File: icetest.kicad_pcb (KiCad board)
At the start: 2 copper layers, 66.7 x 57.2 mm, 61 parts, among them J1 R, J2 R, J3 R

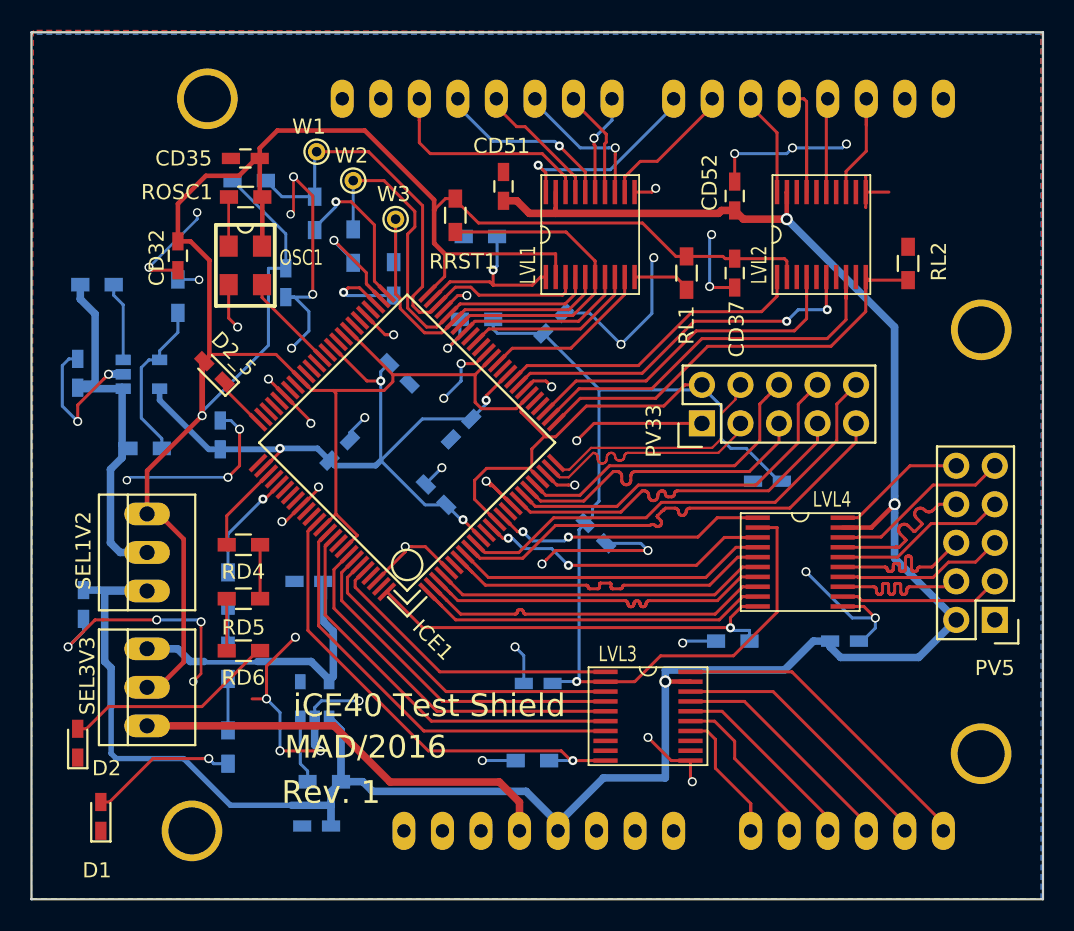
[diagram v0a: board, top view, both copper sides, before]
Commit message: more current for LEDs
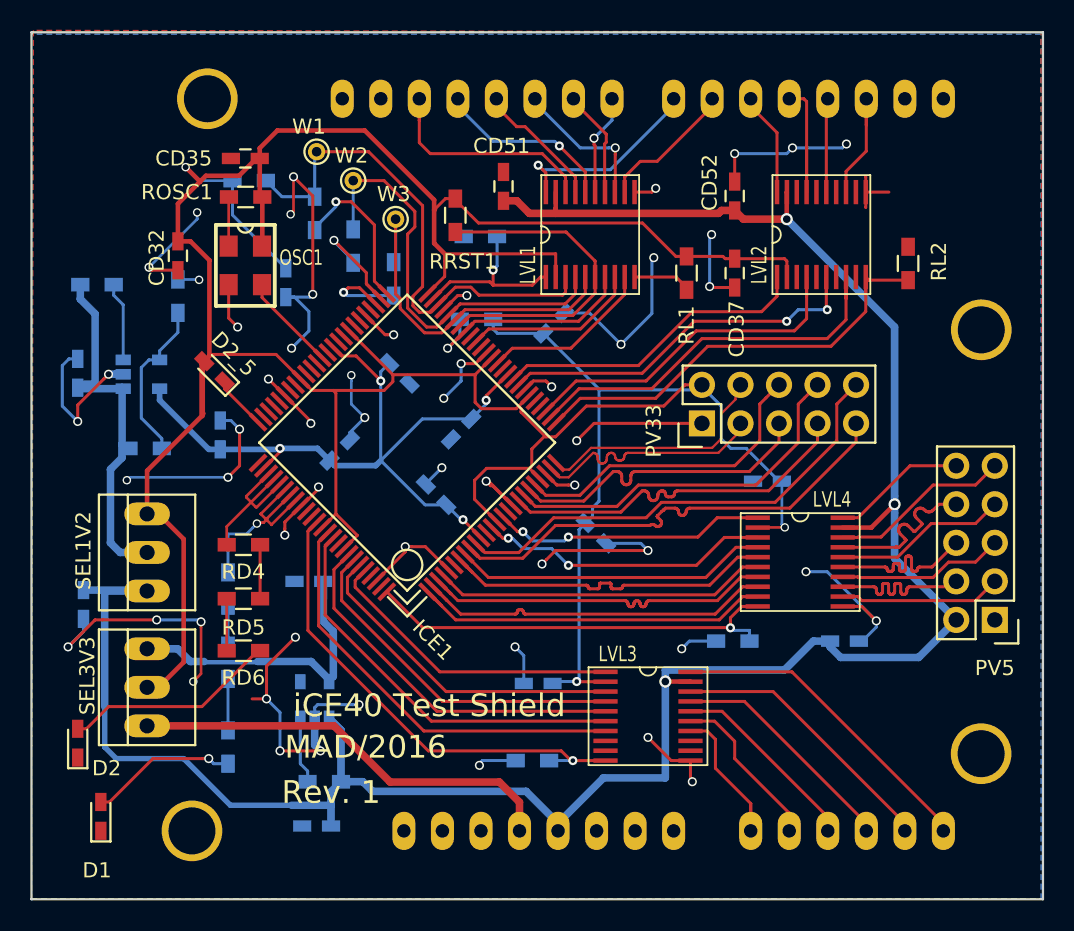
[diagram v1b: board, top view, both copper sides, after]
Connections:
- ICE1 pad 79: Net-(ICE1-Pad79) -> Net-(ICE1-Pad78)
- ICE1 pad 80: Net-(ICE1-Pad80) -> Net-(ICE1-Pad78)
- ICE1 pad 82: Net-(ICE1-Pad82) -> Net-(ICE1-Pad81)
- ICE1 pad 83: Net-(ICE1-Pad83) -> Net-(ICE1-Pad81)
- RD1 pad 1: Net-(ICE1-Pad80) -> Net-(ICE1-Pad81)
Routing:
- net +3V3: track 266.8 -> 243.8 mm, vias 2 -> 3
- net Net-(ICE1-Pad81): track 0.00 -> 13.3 mm, vias 0 -> 1
- net Net-(ICE1-Pad80): track 7.28 -> 0.00 mm, vias 1 -> 0
- net Net-(ICE1-Pad78): track 5.83 -> 10.9 mm
- net GND: track 193.5 -> 198.0 mm, vias 54 -> 55

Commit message: minor layout
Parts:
- removed J1, J2, J3: R, Resistors_SMD:R_0603_HandSoldering
- added W4: CDONE, Connect:PINTST, F.Cu at (146.8, 106.5)
- added W5: RST, Connect:PINTST, F.Cu at (145.7, 103.0)
- CD34, CD38: moved to F.Cu
- W1: value TEST_1P -> SCLK
- W2: value TEST_1P -> MISO
- W3: value TEST_1P -> MOSI
- moved CD34 28.8 mm to (132.7, 118.6), turned to 135 degrees
- moved CD38 28.6 mm to (130.2, 120.7), turned to 135 degrees
- moved RDON1 9.30 mm to (150.7, 103.1)
- moved W1 8.83 mm to (143.1, 110.0)
- moved W3 4.21 mm to (143.0, 106.0)
- moved W2 3.02 mm to (141.8, 101.6)
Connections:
- W2 pad 1: /Arduino Shield/MOSI -> /Arduino Shield/MISO
- W3 pad 1: /Arduino Shield/MISO -> /Arduino Shield/MOSI
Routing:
- net /Arduino Shield/ICE_RST: track 22.9 -> 38.7 mm, vias 0 -> 1
- net /Arduino Shield/ICE_CDONE: track 15.7 -> 27.4 mm
- net Net-(ICE1-Pad51): track 11.0 -> 0.97 mm, vias 1 -> 0
- net (no net): track 0.00 -> 8.85 mm, vias 0 -> 2
- net Net-(ICE1-Pad52): track 8.57 -> 0.00 mm, vias 1 -> 0
- net Net-(ICE1-Pad53): track 6.87 -> 0.00 mm, vias 1 -> 0
- net /Arduino Shield/MOSI: track 28.3 -> 22.8 mm, vias 0 -> 1
- net /Arduino Shield/SCK: track 34.2 -> 28.9 mm, vias 0 -> 1
- net +3V3: track 243.8 -> 249.0 mm, vias 3 -> 5
- net /Arduino Shield/MISO: track 24.0 -> 28.7 mm, vias 0 -> 1
- net GND: track 198.0 -> 193.9 mm, vias 55 -> 54
- net VCC: track 50.4 -> 51.7 mm
- net /Arduino Shield/aSCK: track 15.9 -> 15.1 mm

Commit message: add errata and notes
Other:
- board text added: "33V"
- board text added: "5V"
- board text added: "CDNE"
- board text added: "GND"
- board text added: "MISO"
- board text added: "MOSI"
- board text added: "RST"
- board text added: "SCK"
- board text added: "a33V"
- board text added: "r33V"
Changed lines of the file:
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@@
     (links 206)
     (no_connects 0)
-    (area 123.114999 93.269999 189.940001 150.570001)
+    (area 117.115001 50.227999 191.801534 156.163599)
     (thickness 1.6)
-    (drawings 11)
+    (drawings 26)
     (tracks 1805)
     (zones 0)
@@
     (pad_to_mask_clearance 0.2)
     (aux_axis_origin 0 0)
-    (visible_elements FFFFFF79)
+    (visible_elements FFFFFE79)
     (pcbplotparams
-      (layerselection 0x00030_80000001)
+      (layerselection 0x00120_00000001)
       (usegerberextensions false)
       (excludeedgelayer true)
@@
       (outputformat 4)
       (mirror false)
-      (drillshape 0)
+      (drillshape 2)
       (scaleselection 1)
-      (outputdirectory ""))
+      (outputdirectory /tmp))
   )
   (net 0 "")
@@
     )
   )
+  (gr_text 5V (at 120.269 130.4798) (layer Dwgs.User)
+    (effects (font (size 1.5 1.5) (thickness 0.3)))
+  )
+  (gr_text 33V (at 120.4214 125.1966) (layer Dwgs.User)
+    (effects (font (size 1.5 1.5) (thickness 0.3)))
+  )
+  (gr_text a33V (at 120.015 138.9126) (layer Dwgs.User)
+    (effects (font (size 1.5 1.5) (thickness 0.3)))
+  )
+  (gr_text 33V (at 120.3706 136.652) (layer Dwgs.User)
+    (effects (font (size 1.5 1.5) (thickness 0.3)))
+  )
+  (gr_text r33V (at 119.9134 134.1374) (layer Dwgs.User)
+    (effects (font (size 1.5 1.5) (thickness 0.3)))
+  )
+  (gr_text a33V (at 155.3972 153.2636 90) (layer Dwgs.User)
+    (effects (font (size 1.5 1.5) (thickness 0.3)))
+  )
+  (gr_text 5V (at 158.0134 153.3144 90) (layer Dwgs.User)
+    (effects (font (size 1.5 1.5) (thickness 0.3)))
+  )
+  (gr_text GND (at 163.1696 153.2636 90) (layer Dwgs.User)
+    (effects (font (size 1.5 1.5) (thickness 0.3)))
+  )
+  (gr_text GND (at 160.528 153.3398 90) (layer Dwgs.User)
+    (effects (font (size 1.5 1.5) (thickness 0.3)))
+  )
+  (gr_text RST (at 161.4678 90.17 90) (layer Dwgs.User)
+    (effects (font (size 1.5 1.5) (thickness 0.3)))
+  )
+  (gr_text CDNE (at 158.9532 90.1954 90) (layer Dwgs.User)
+    (effects (font (size 1.5 1.5) (thickness 0.3)))
+  )
+  (gr_text MOSI (at 153.8478 90.1446 90) (layer Dwgs.User)
+    (effects (font (size 1.5 1.5) (thickness 0.3)))
+  )
+  (gr_text MISO (at 151.3332 90.17 90) (layer Dwgs.User)
+    (effects (font (size 1.5 1.5) (thickness 0.3)))
+  )
+  (gr_text SCK (at 148.8948 90.551 90) (layer Dwgs.User)
+    (effects (font (size 1.5 1.5) (thickness 0.3)))
+  )
+  (gr_text GND (at 146.2786 90.424 90) (layer Dwgs.User)
+    (effects (font (size 1.5 1.5) (thickness 0.3)))
+  )
   (gr_text "Rev. 1" (at 174.117 109.4105) (layer B.SilkS)

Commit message: redo layout
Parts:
- removed LVL1, LVL2, LVL3, LVL4: txb0108, local:PSO_20
- removed RCLK1, RL1, RL2, RL3, RL4: 10k, Resistors_SMD:R_0603_HandSoldering
- added P0: CONN_02X04, Pin_Headers:Pin_Header_Straight_2x05, F.Cu at (161.5, 141.2)
- added P11: CONN_02X04, Pin_Headers:Pin_Header_Straight_2x05, F.Cu at (139.2, 106.2)
- added P12: CONN_02X04, Pin_Headers:Pin_Header_Straight_2x05, F.Cu at (138.7, 133.1)
- added P2: CONN_02X04, Pin_Headers:Pin_Header_Straight_2x05, F.Cu at (185.9, 102.6)
- added RSCK1: 10k, Resistors_SMD:R_0603_HandSoldering, F.Cu at (144.8, 103.6)
- added RU3: 10k, Resistors_SMD:R_0603_HandSoldering, B.Cu at (161.0, 108.3)
- added RU4: 10k, Resistors_SMD:R_0603_HandSoldering, F.Cu at (168.1, 104.1)
- added UL1: sn74lvc2t45, local:VSSOP-8, F.Cu at (148.6, 104.1)
- added UL2: sn74lvc2t45, local:VSSOP-8, F.Cu at (153.7, 104.1)
- added UL3: sn74lvc2t45, local:VSSOP-8, F.Cu at (158.8, 104.1)
- added UL4: sn74lvc2t45, local:VSSOP-8, F.Cu at (163.8, 104.1)
- added UL5: sn74lvc2t45, local:VSSOP-8, F.Cu at (176.3, 137.2)
- added UL6: sn74lvc2t45, local:VSSOP-8, F.Cu at (177.3, 132.6)
- added UL7: sn74lvc2t45, local:VSSOP-8, F.Cu at (175.3, 128.3)
- added UL8: sn74lvc2t45, local:VSSOP-8, F.Cu at (177.3, 124.5)
- added W12: TEST_1P, Connect:PINTST, F.Cu at (135.6, 120.4)
- CD32, CD34, CD37, CD38, CD51, D2_5, RRST1: moved to B.Cu
- CD53: moved to F.Cu
- SEL1V2, SEL3V3: footprint Connect:PINHEAD1-3 -> Pin_Headers:Pin_Header_Straight_1x03
- moved CD53 52.7 mm to (178.3, 141.2), turned to 0 degrees
- moved CD34 43.3 mm to (172.2, 136.1), turned to 180 degrees
- moved CD32 30.4 mm to (155.8, 128.0), turned to 90 degrees
- moved CD38 28.5 mm to (158.7, 121.8), turned to 270 degrees
- moved D2 21.1 mm to (147.2, 142.5), turned to 0 degrees
- moved D2_5 20.7 mm to (144.8, 134.1), turned to 270 degrees
- moved RD1 17.7 mm to (152.9, 135.6), turned to 0 degrees
- moved OSC1 17.6 mm to (140.7, 126.0)
- moved RD4 17.5 mm to (152.4, 135.6)
- moved CD54 17.2 mm to (184.9, 118.4), turned to 90 degrees
- moved RD2 17.1 mm to (152.9, 138.2), turned to 180 degrees
- moved ROSC1 17.0 mm to (140.7, 120.9)
- moved RD5 17.0 mm to (152.4, 138.2)
- moved RD3 16.8 mm to (152.9, 140.7), turned to 0 degrees
- moved CD36 16.6 mm to (151.2, 120.5), turned to 270 degrees
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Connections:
- ARD1 pad 20: Net-(ARD1-Pad20) -> /Arduino Shield/aD5
- ARD1 pad 22: /Arduino Shield/aD7 -> Net-(ARD1-Pad22)
- ICE1 pad 10: /FPGA/D5- -> /FPGA/DIR5
- ICE1 pad 100: Net-(ICE1-Pad100) -> /FPGA/DIR1
- ICE1 pad 12: Net-(ICE1-Pad12) -> /FPGA/D5+
- ICE1 pad 13: Net-(ICE1-Pad13) -> /FPGA/D5-
- ICE1 pad 15: Net-(ICE1-Pad15) -> /FPGA/D7+
- ICE1 pad 16: Net-(ICE1-Pad16) -> /FPGA/D7-
- ICE1 pad 26: /Arduino Shield/LOG_L2E -> Net-(ICE1-Pad26)
- ICE1 pad 27: /Arduino Shield/DIG2 -> Net-(ICE1-Pad27)
- ICE1 pad 28: /Arduino Shield/DIG4 -> Net-(ICE1-Pad28)
- ICE1 pad 33: /Arduino Shield/DIG3 -> Net-(ICE1-Pad33)
- ICE1 pad 34: /Arduino Shield/DIG5 -> Net-(ICE1-Pad34)
- ICE1 pad 37: /Arduino Shield/DIG6 -> Net-(ICE1-Pad37)
- ICE1 pad 40: Net-(ICE1-Pad40) -> /Arduino Shield/DD
- ICE1 pad 41: /Arduino Shield/DIG10 -> /Arduino Shield/D5
- ICE1 pad 42: Net-(ICE1-Pad42) -> /Arduino Shield/D6
- ICE1 pad 79: Net-(ICE1-Pad78) -> Net-(ICE1-Pad79)
- ICE1 pad 80: Net-(ICE1-Pad78) -> Net-(ICE1-Pad80)
- ICE1 pad 81: Net-(ICE1-Pad81) -> Net-(ICE1-Pad80)
- ICE1 pad 82: Net-(ICE1-Pad81) -> Net-(ICE1-Pad80)
- ICE1 pad 83: Net-(ICE1-Pad81) -> Net-(ICE1-Pad83)
- ICE1 pad 85: Net-(ICE1-Pad85) -> Net-(ICE1-Pad83)
- ICE1 pad 86: Net-(ICE1-Pad86) -> Net-(ICE1-Pad83)
- ICE1 pad 87: /Arduino Shield/LOG_L3E -> /FPGA/P01
- ICE1 pad 89: /Arduino Shield/ANA0 -> Net-(ICE1-Pad89)
- ICE1 pad 9: /FPGA/D5+ -> /FPGA/DIR3
- ICE1 pad 90: /Arduino Shield/ANA1 -> Net-(ICE1-Pad90)
- ICE1 pad 93: /Arduino Shield/ANA2 -> Net-(ICE1-Pad93)
- ICE1 pad 94: /Arduino Shield/ANA3 -> Net-(ICE1-Pad94)
- ICE1 pad 95: /Arduino Shield/ANA4 -> Net-(ICE1-Pad95)
- ICE1 pad 96: /Arduino Shield/ANA5 -> Net-(ICE1-Pad96)
- ICE1 pad 99: Net-(ICE1-Pad99) -> /FPGA/DIR2
- PV33 pad 10: /FPGA/D5- -> /FPGA/D7-
- PV33 pad 9: /FPGA/D5+ -> /FPGA/D7+
- PV5 pad 10: Net-(LVL4-Pad20) -> /FPGA/xD5-
- PV5 pad 9: Net-(LVL4-Pad18) -> /FPGA/xD5+
- RD1 pad 1: Net-(ICE1-Pad81) -> Net-(ICE1-Pad83)
- RD4 pad 1: Net-(ICE1-Pad78) -> Net-(ICE1-Pad80)
- RRST1 pad 1: /Arduino Shield/ICE_RST -> /Arduino Shield/aD9
- RRST1 pad 2: +3V3 -> +5V
- RSS1 pad 1: GND -> /Arduino Shield/aD10
- RSS1 pad 2: /Arduino Shield/ICE_SS -> GND
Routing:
- net +5V: track 154.1 -> 218.2 mm, vias 3 -> 4
- net GND: track 193.9 -> 135.8 mm, vias 54 -> 51
- net +3V3: track 249.0 -> 282.7 mm, vias 5 -> 10
- net Net-(ICE1-Pad27): track 0.00 -> 32.2 mm
- net /Arduino Shield/LOG_L3E: track 32.1 -> 0.00 mm, vias 1 -> 0
- net Net-(ICE1-Pad29): track 0.00 -> 31.1 mm
- net Net-(ICE1-Pad33): track 0.00 -> 30.1 mm
- net /Arduino Shield/LOG_L2E: track 29.7 -> 0.00 mm
- net Net-(ICE1-Pad26): track 0.00 -> 28.9 mm
- net /Arduino Shield/ANA0: track 28.6 -> 0.00 mm
- net Net-(ICE1-Pad36): track 0.00 -> 28.5 mm
- net Net-(ICE1-Pad100): track 28.5 -> 0.00 mm, vias 1 -> 0
- net Net-(ICE1-Pad28): track 0.00 -> 28.4 mm
- net Net-(ICE1-Pad30): track 0.00 -> 27.2 mm
- net /Arduino Shield/ANA1: track 27.0 -> 0.00 mm
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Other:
- board text added: "+3.3"
- board text added: "+5"
- board text added: "D5"
- board text added: "D6"
- board text added: "DONE"
- board text added: "Rev. 2"
- board text added: "SS"
- board text removed: "33V"
- board text removed: "Rev. 1"
- board text removed: "r33V"

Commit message: more layout
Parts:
- added CR4: 1u, Capacitors_SMD:C_0603_HandSoldering, F.Cu at (133.0, 137.8)
- added W6: SS, Connect:PINTST, F.Cu at (148.1, 113.3)
- R122, R123: value R -> 10k
- moved D2_5 1.33 mm to (146.1, 134.1)
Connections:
- net /FPGA/D5+ renamed /FPGA/D6+
- net /FPGA/D5- renamed /FPGA/D6-
- net /FPGA/DIR5 renamed /FPGA/DIR6
- net /FPGA/xD5+ renamed /FPGA/xD6+
- net /FPGA/xD5- renamed /FPGA/xD6-
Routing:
- net GND: track 135.8 -> 146.5 mm, vias 51 -> 53
- net +5V: track 218.2 -> 211.6 mm
- net /Arduino Shield/ICE_SS: track 13.1 -> 15.6 mm
- net +3V3: track 282.7 -> 284.1 mm
- net Net-(D2_5-Pad1): track 4.89 -> 3.56 mm
- net /Arduino Shield/a3V3: track 38.4 -> 39.6 mm
- net /FPGA/DIR3: track 17.6 -> 16.7 mm
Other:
- board text added: "1"
- board text added: "12"
- board text added: "13"
- board text added: "15"
- board text added: "16"
- board text added: "18"
- board text added: "19"
- board text added: "2"
- board text added: "20"
- board text added: "21"
- board text added: "24"
- board text added: "25"
- board text added: "26"
- board text added: "27"
- board text added: "28"
- board text added: "29"
- board text added: "3"
- board text added: "30"
- board text added: "33"
- board text added: "34"
- board text added: "36"
- board text added: "4"
- board text added: "51"
- board text added: "52"
- board text added: "53"
- board text added: "54"
- board text added: "56"
- board text added: "57"
- board text added: "59"
- board text added: "60"
- board text added: "64"
- board text added: "65"
- board text added: "66"
- board text added: "68"
- board text added: "69"
- board text added: "7"
- board text added: "71"
- board text added: "72"
- board text added: "73"
- board text added: "8"
- board text added: "87"
- board text added: "89"
- board text added: "90"
- board text added: "93"
- board text added: "94"
- board text added: "95"
- board text added: "96"
- board text added: "97"
- board text added: "D10"
- board text added: "D100"
- board text added: "D9"
- board text added: "D99"
- board text added: "a33"
- board text added: "iVcc"
- board text added: "r33"
- board text removed: "5V"
- board text removed: "CDNE"
- board text removed: "a33V"

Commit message: more layout
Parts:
- added RDR1: 10k, Resistors_SMD:R_0603_HandSoldering, B.Cu at (178.4, 136.0)
- added RDR2: 10k, Resistors_SMD:R_0603_HandSoldering, B.Cu at (171.8, 130.2)
- added RDR3: 10k, Resistors_SMD:R_0603_HandSoldering, B.Cu at (176.5, 128.7)
- added RDR6: 10k, Resistors_SMD:R_0603_HandSoldering, B.Cu at (167.9, 124.8)
- added W7: CLK, Measurement_Points:Measurement_Point_Square-SMD-Pad_Small, F.Cu at (144.1, 123.8)
- P0, P11, P12, P2: value CONN_02X04 -> CONN_02X05
- W1, W12, W2, W3, W4, W5, W6: footprint Connect:PINTST -> Measurement_Points:Measurement_Point_Square-SMD-Pad_Small
- moved RRST1 13.6 mm to (163.6, 102.4)
- moved W6 4.97 mm to (152.1, 110.4)
- moved W3 4.36 mm to (150.1, 112.7)
- moved W2 4.04 mm to (156.4, 110.2)
- moved RSS1 3.37 mm to (152.8, 104.1)
- moved RDON1 1.71 mm to (155.3, 110.4)
- moved W5 1.53 mm to (154.3, 112.5)
- moved W1 0.97 mm to (148.1, 110.4)
- moved W4 0.66 mm to (158.5, 112.4)
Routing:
- net GND: track 146.5 -> 152.4 mm
- net VCC: track 63.5 -> 66.3 mm, vias 4 -> 5
- net /Arduino Shield/MOSI: track 15.2 -> 12.7 mm
- net +3V3: track 284.1 -> 285.5 mm
- net /FPGA/DIR3: track 16.7 -> 17.9 mm
- net /Arduino Shield/ICE_SS: track 15.6 -> 14.4 mm
- net /FPGA/CLK: track 7.20 -> 8.34 mm
- net /Arduino Shield/ICE_RST: track 13.2 -> 12.1 mm, vias 2 -> 0
- net /Arduino Shield/MISO: track 15.7 -> 14.6 mm, vias 1 -> 2
- net /Arduino Shield/aD5: track 10.0 -> 9.03 mm
- net /Arduino Shield/DD: track 24.4 -> 25.2 mm
- net /Arduino Shield/aD9: track 14.9 -> 14.1 mm, vias 1 -> 0
- net /FPGA/DIR1: track 22.1 -> 22.8 mm
- net /FPGA/DIR2: track 20.7 -> 21.4 mm
- net /FPGA/DIR6: track 16.1 -> 16.8 mm
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
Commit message: more layout
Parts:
- W12: value TEST_1P -> +1.2
- moved CD11 4.58 mm to (147.8, 124.7), turned to 270 degrees
- moved D2_5 3.03 mm to (145.1, 131.3), turned to 90 degrees
- moved CD38 2.25 mm to (159.9, 119.9), turned to 90 degrees
- moved CD12 2.11 mm to (155.2, 120.0), turned to 90 degrees
- moved CD36 2.03 mm to (151.1, 118.5), turned to 90 degrees
- moved CD13 1.93 mm to (152.3, 129.9), turned to 270 degrees
- moved CD14 1.92 mm to (161.4, 124.7), turned to 0 degrees
- moved CD32 1.62 mm to (157.3, 128.7), turned to 0 degrees
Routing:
- net GND: track 152.4 -> 165.5 mm, vias 53 -> 52
- net +3V3: track 285.5 -> 282.6 mm
- net Net-(ICE1-Pad29): track 31.1 -> 28.4 mm
- net Net-(ICE1-Pad30): track 27.2 -> 24.7 mm
- net Net-(ICE1-Pad28): track 28.4 -> 26.1 mm
- net Net-(ICE1-Pad33): track 30.1 -> 27.8 mm
- net Net-(ICE1-Pad27): track 32.2 -> 29.9 mm
- net Net-(ICE1-Pad34): track 26.3 -> 24.1 mm
- net Net-(ICE1-Pad36): track 28.5 -> 26.8 mm
- net Net-(ICE1-Pad26): track 28.9 -> 27.5 mm
- net Net-(D2_5-Pad1): track 3.56 -> 4.18 mm
- net Net-(ICE1-Pad73): track 17.5 -> 17.0 mm

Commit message: more layout
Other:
- board text added: "63"
